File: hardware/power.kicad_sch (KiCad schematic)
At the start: 42 parts, among them J401 61300111121, J402 61300111121, J403 PRPC001DAAN-RC, J404 61300111121, J405 PRPC001DAAN-RC, J406 PRPC001DAAN-RC, J407 61300111121, Q401 BSS806NH, U401 LM66200DRLR, U402 TPS63020DSJR, U403 LD39200DPUR

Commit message: HW: Refactor the schematics
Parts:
- removed C410: 0.1 µF, perfect_footprints:C_0402_1005Metric, symbol Device:C
- removed C411: 10 μF, Capacitor_SMD:C_0603_1608Metric, symbol Device:C
- removed D401: 150141RS73100, LED_SMD:LED_PLCC_2835, symbol Device:LED
- removed J402: 61300111121, Connector_PinHeader_2.54mm:PinHeader_1x01_P2.54mm_Vertical, symbol Connector_Generic:Conn_01x01
- removed J403: PRPC001DAAN-RC, Connector_PinHeader_2.54mm:PinHeader_1x02_P2.54mm_Vertical, symbol Connector_Generic:Conn_01x02
- removed Q401: BSS806NH, Package_TO_SOT_SMD:SOT-23-3, symbol Transistor_FET:Q_NMOS_GSD
- removed R402, R404: 330 Ω, perfect_footprints:R_0402_1005Metric, symbol Device:R
- removed R403: 180 kΩ, perfect_footprints:R_0402_1005Metric, symbol Device:R
- removed R405, R413: 0 Ω, perfect_footprints:R_0402_1005Metric, symbol Device:R
- removed R410: 56 kΩ, perfect_footprints:R_0402_1005Metric, symbol Device:R
- removed R411: 10 kΩ, perfect_footprints:R_0402_1005Metric, symbol Device:R
- removed R412: 4.7 kΩ, perfect_footprints:R_0402_1005Metric, symbol Device:R
- removed TP401: TestPoint, TestPoint:TestPoint_Pad_D1.0mm, symbol Connector:TestPoint
- removed U403: LD39200DPUR, Package_DFN_QFN:DFN-8-1EP_4x4mm_P0.8mm_EP2.3x3.24mm, symbol STMicroelectronics:LD39200DPUR
- added C203, C204: 1 µF, Capacitor_SMD:C_0603_1608Metric, symbol Device:C
- added C301: 100 μF, Capacitor_THT:CP_Radial_D5.0mm_P2.00mm, symbol Device:C_Polarized
- added C302, C305: 0.1 µF, perfect_footprints:C_0402_1005Metric, symbol Device:C
- added C303, C304: 4.7 µF, Capacitor_SMD:C_0603_1608Metric, symbol Device:C
- added D301, D302, D303: 150141RS73100, LED_SMD:LED_PLCC_2835, symbol Device:LED
- added D704: SMAJ5.0A, Diode_SMD:D_SMA, symbol Device:D_Zener
- added D705: DT1240A-08LP3810-7, Package_DFN_QFN:Diodes_UDFN3810-9_TYPE_B, symbol Power_Protection:D3V3X8U9LP3810
- added F201, F301: 1.5A, Fuse:Fuse_0805_2012Metric, symbol Device:Fuse
- added J1: USB4105-GF-A, Connector_USB:USB_C_Receptacle_GCT_USB4105-xx-A_16P_TopMnt_Horizontal, symbol Connector:USB_C_Receptacle_USB2.0_16P
- added J202, J302: PRPC001DAAN-RC, Connector_PinHeader_2.54mm:PinHeader_1x02_P2.54mm_Vertical, symbol Connector_Generic:Conn_01x02
- added J301: B2B-XH-A, Connector_JST:JST_XH_B2B-XH-A_1x02_P2.50mm_Vertical, symbol Connector_Generic:Conn_01x02
- added L301: 1.5 µH, Inductor_SMD:L_Vishay_IHLP-2525, symbol Device:L
- added Q301: IRLML6401TRPBF, Package_TO_SOT_SMD:SOT-23-3, symbol Transistor_FET:Q_PMOS_GSD
- added Q302, Q303: DMN2005, Package_SON:Diodes_PowerDI3333-8, symbol Diodes Incorporated:DMN2005UFG-7
- added R103: 0 Ω, Resistor_SMD:R_1206_3216Metric, symbol Device:R
- added R301: 330 Ω, perfect_footprints:R_0402_1005Metric, symbol Device:R
- added R302: 82 mΩ, Resistor_SMD:R_1206_3216Metric, symbol Device:R
- added R303, R305: 2.2 kΩ, perfect_footprints:R_0402_1005Metric, symbol Device:R
- added R304: 10 kΩ, perfect_footprints:R_0402_1005Metric, symbol Device:R
- added R306, R307, R308: 4.7 kΩ, perfect_footprints:R_0402_1005Metric, symbol Device:R
- added R309: 22 Ω, perfect_footprints:R_0402_1005Metric, symbol Device:R
- added R710, R711: 5.1 kΩ, perfect_footprints:R_0402_1005Metric_HDI, symbol Device:R
- added TP301, TP302, TP404: TestPoint, TestPoint:TestPoint_Pad_D1.0mm, symbol Connector:TestPoint
- added U301: BQ29728DSER, Package_SON:WSON-6_1.5x1.5mm_P0.5mm, symbol Texas Instruments:BQ297xy
- added U302: MCP73833T-FCI/MF, Package_DFN_QFN:DFN-10-1EP_3x3mm_P0.5mm_EP1.58x2.35mm, symbol Battery_Management:MCP73833-xxx-MF
- added U303: MAX17048G+T10, Package_DFN_QFN:TDFN-8-1EP_2x2mm_P0.5mm_EP0.8x1.2mm, symbol Analog Devices:MAX17048
- C409: value 10 μF -> 4.7 µF; DigiKey Part Number 490-12737-1-ND -> 490-7203-1-ND; MPN GRM188R61E106MA73J -> GRM188R61E475KE11D; Size 0603 -> 0402; Tolerance ≤ 20 % -> ≤ 20%; Voltage ≥ 16 V -> ≥ 10 V
- R409: value 1.1 MΩ -> 0 Ω; DigiKey Part Number 732-560112110179CT-ND -> 732-560112110001CT-ND; MPN 560112110179 -> 560112110001; Size (none) -> 0402; Tolerance ≤ 1 % -> (none); now not fitted; now left out of the parts list
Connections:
- net ST is gone; now on net BAT_DETn: R401.2, U401.8 (ST)
- net BAT_DETn: now also C409.1
- net GND: now also C203.2, C204.2, C303.2, C304.2, C305.2, J1.A1 (GND), J1.A12 (GND), J1.B1 (GND), J1.B12 (GND), J202.1 (Pin_1), J302.2 (Pin_2), Q303.1 (S), Q303.2 (S), Q303.3 (S), R303.2, R304.2, R305.2, R710.2, R711.2, U302.11 (EP), U302.5 (V_{SS}), U303.1 (CTG), U303.4 (GND), U303.6 (QSTRT), U303.9 (EP)
- net PS/SYNC: now also R409.1
- net VINA: now also R409.2
- net V_3V3: now also R103.2
- net V_BAT: now also C301.1, C303.1, C305.1, Q301.2 (S), R301.1, TP404.1, U302.10 (V_{BAT}), U302.9 (V_{BAT}), U303.2 (CELL), U303.3 (V_{DD})
- net V_3V3_EN: no longer names the net of U402.14 (PG)
- net V_3V3_EN: no longer R409.2
- net V_3V3_OUT: no longer names the net of J405.1 (Pin_1)
- net V_3V3_OUT: now also C406.1, C407.1, C408.1, R407.1, U402.4 (VOUT), U402.5 (VOUT), R103.1
- removed net V_3V55: C406.1, C407.1, C408.1, C409.1, R407.1, R409.1, U402.4 (VOUT), U402.5 (VOUT)
- net V_5V0 renamed V_BUS
- net V_BUS: now also C204.1, C304.1, D301.2 (A), D302.2 (A), D303.2 (A), J202.2 (Pin_2), L301.2, U302.1 (V_{DD}), U302.2 (V_{DD})
- new net: D303.1 (K), R308.2
- new net: C301.2, C302.2, J301.1 (Pin_1), Q301.1 (G), R302.1, U301.4 (VSS)
- new net: J302.1 (Pin_1), Q302.1 (S), Q302.2 (S), Q302.3 (S), R302.2
- new net: D301.1 (K), R306.2
- new net: C203.1, F201.2, L301.1
- new net: R309.1, U303.5 (~{ALRT})
- new net: F301.2, Q301.3 (D)
- new net: D302.1 (K), R307.2
- new net: Q302.5 (D), Q303.5 (D)
- new net BAT_MON_INTn: R309.2
- new net BAT_PROT_IN: C302.1, R301.2, U301.5 (BAT)
- new net CC1: J1.A5 (CC1), R711.1
- new net CC2: J1.B5 (CC2), R710.1
- new net CHASSIS: D704.2 (A), D705.3 (GND), J1.SH (SHIELD)
- new net C_{OUT}: Q303.4 (G), TP302.1, U301.2 (Cout)
- new net D_{OUT}: Q302.4 (G), TP301.1, U301.3 (Dout)
- new net I2C.SCL: U303.7 (SCL)
- new net I2C.SDA: U303.8 (SDA)
- new net PG: R308.1, U302.7 (~{PG})
- new net PROG: R305.1, U302.6 (PROG)
- new net STAT1: R306.1, U302.3 (STAT1)
- new net STAT2: R307.1, U302.4 (STAT2)
- new net THERM: R304.1, U302.8 (THERM)
- new net USB.DM: D705.1 (Line-1), J1.A7 (D-), J1.B7 (D-)
- new net USB.DP: D705.2 (Line-3), J1.A6 (D+), J1.B6 (D+)
- new net V-: R303.1, U301.6 (V-)
- new net V_BAT_IN: F301.1, J301.2 (Pin_2)
- new net V_BUS_IN: D704.1 (K), F201.1, J1.A4 (VBUS), J1.A9 (VBUS), J1.B4 (VBUS), J1.B9 (VBUS)
- no-connect marks 0 -> 10
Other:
- note added: "Battery"
- note added: "Charging"
- note added: "Debug"
- note added: "Monitoring"
- note added: "Notes"
- note added: "OPT: Bypass protection chip"
- note added: "OPT: External +5V supply"
- note added: "Power path management"
- note added: "Power regulation"
- note added: "Protection"
- note added: "R1"
- note added: "R2"
- note added: "Route USB as 90 Ω differential."
- note added: "USB"
- note removed: "If the board is powered from V_BAT, then ST is pulled high. If the board is powered from V_5V0, then ST is pulled low. BAT_DETn is low when the battery is providing the power. BAT_DETn is high when the USB is providing the power."
- note removed: "Max dropout voltage is 250 mV according to datasheet."
- note removed: "Place close to LDO."
- note removed: "Place the header near the test points for the oscilloscope ground."
- note removed: "Power path management If V_BAT > V_5V0, V_{OUT} = V_BAT If V_5V0 > V_BAT, V_{OUT} = V_5V0"
- note removed: "Testing: For current measurements, populate the header and remove the 0 Ω jumper."
- note removed: "Testing: Power-saving mode should be enabled but if it doesn't work, provide an easy way to disable it."
- note removed: "Use a common center pad."
- note removed: "V_{OUT} will be 3.55 V, which is just enough for the LDO."
- moved on the sheet: C401, C402, C403, C404, C405, C406, C407, C408, D402, J401, J404, J405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

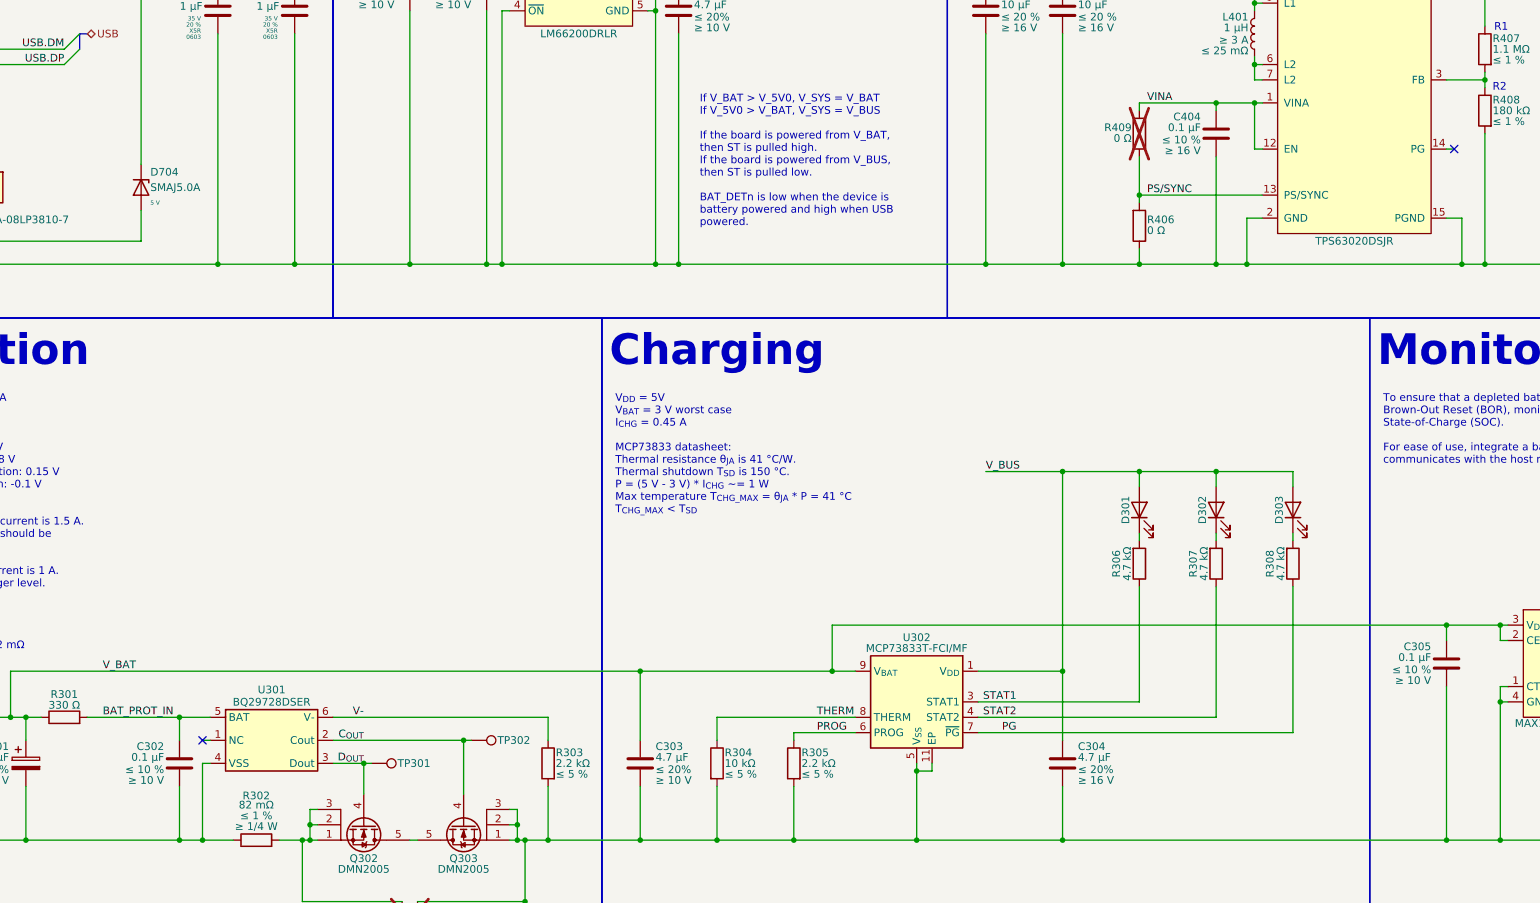
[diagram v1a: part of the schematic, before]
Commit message: Add EEPROM
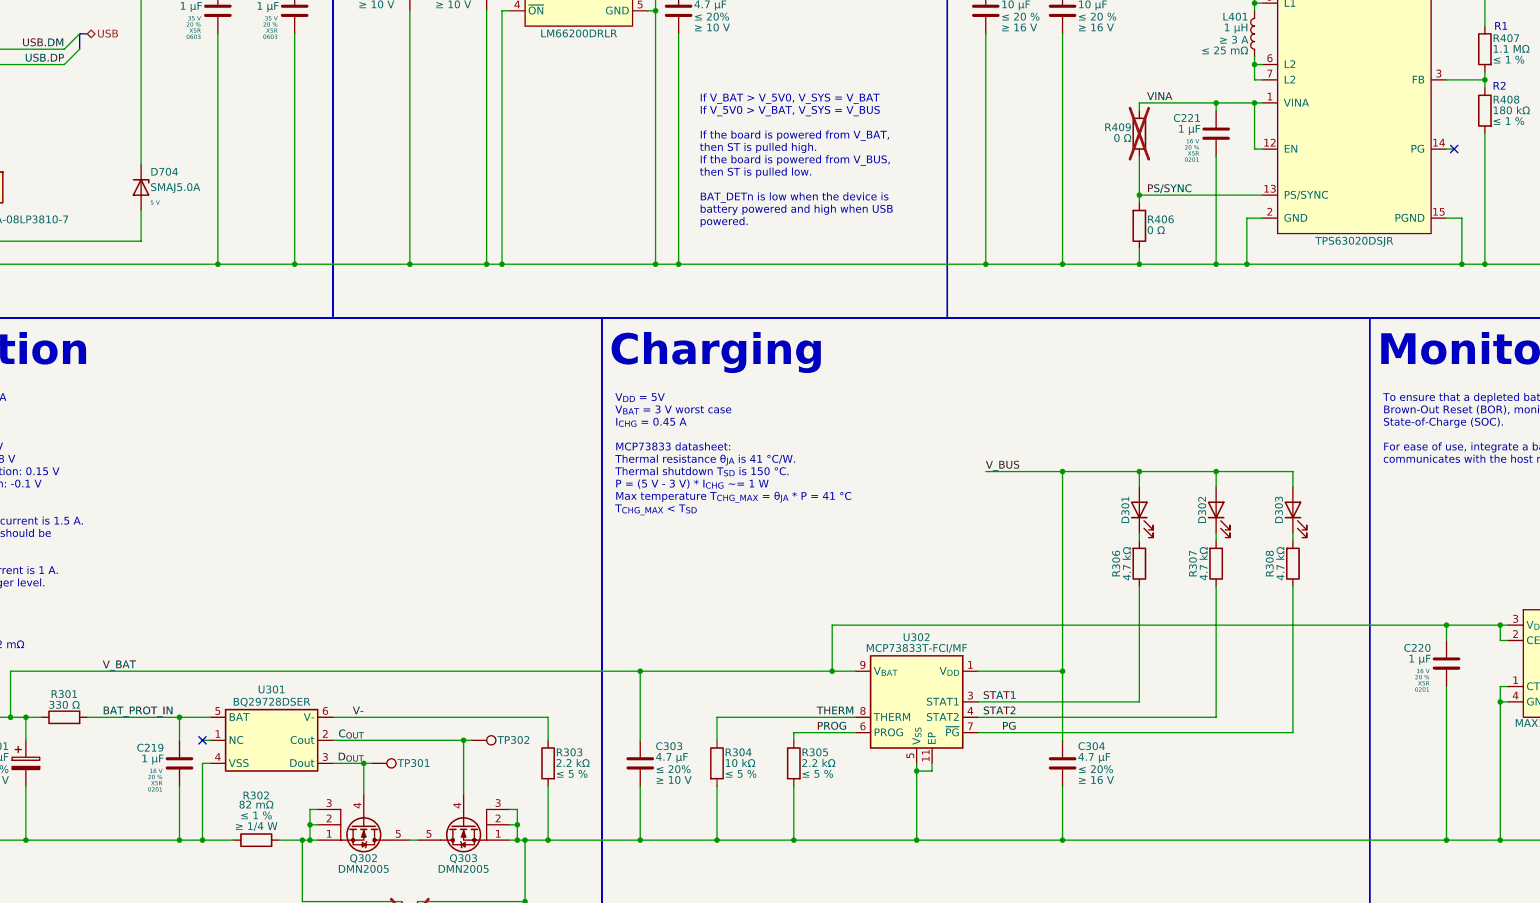
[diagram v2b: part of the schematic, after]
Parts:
- removed C302, C305, C404: 0.1 µF, perfect_footprints:C_0402_1005Metric, symbol Device:C
- added C219, C220, C221: 1 µF, perfect_footprints:C_0201_0603Metric, symbol Device:C
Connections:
- net BAT_PROT_IN: now also C219.1
- net GND: now also C220.2, C221.2
- net VINA: now also C221.1
- net V_BAT: now also C220.1
- net at C301.2, J301.1 (Pin_1), Q301.1 (G)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: now also C219.2

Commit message: Refine schematics
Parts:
- removed C203: 1 µF, Capacitor_SMD:C_0603_1608Metric, symbol Device:C
- removed C301: 100 μF, Capacitor_THT:CP_Radial_D5.0mm_P2.00mm, symbol Device:C_Polarized
- removed C303, C304, C401, C402, C409: 4.7 µF, Capacitor_SMD:C_0603_1608Metric, symbol Device:C
- removed C403, C405: 10 μF, Capacitor_SMD:C_0603_1608Metric, symbol Device:C
- removed C406, C407, C408: 22 μF, Capacitor_SMD:C_0603_1608Metric, symbol Device:C
- removed F201, F301: 1.5A, Fuse:Fuse_0805_2012Metric, symbol Device:Fuse
- removed L401: 1 µH, Inductor_SMD:L_Wuerth_MAPI-4030, symbol Device:L
- removed R301: 330 Ω, perfect_footprints:R_0402_1005Metric, symbol Device:R
- removed R302: 82 mΩ, Resistor_SMD:R_1206_3216Metric, symbol Device:R
- removed R303, R305, R414: 2.2 kΩ, perfect_footprints:R_0402_1005Metric, symbol Device:R
- removed R304: 10 kΩ, perfect_footprints:R_0402_1005Metric, symbol Device:R
- removed R306, R307, R308: 4.7 kΩ, perfect_footprints:R_0402_1005Metric, symbol Device:R
- removed R309: 22 Ω, perfect_footprints:R_0402_1005Metric, symbol Device:R
- removed R401, R408: 180 kΩ, perfect_footprints:R_0402_1005Metric, symbol Device:R
- removed R406, R409: 0 Ω, perfect_footprints:R_0402_1005Metric, symbol Device:R
- removed R407: 1.1 MΩ, perfect_footprints:R_0402_1005Metric, symbol Device:R
- added C1: 100 µF, Capacitor_THT:CP_Radial_D5.0mm_P2.50mm, symbol Device:C_Polarized
- added C10, C4, C9: 10 µF, Capacitor_SMD:C_0603_1608Metric, symbol Device:C
- added C11, C5, C6, C7, C8: 4.7 µF, perfect_footprints:C_0402_1005Metric_HDI, symbol Device:C
- added C14, C15, C16: 22 µF, Capacitor_SMD:C_0603_1608Metric, symbol Device:C
- added D1, D2: SMAJ5.0A, Diode_SMD:D_SMA, symbol Device:D_Zener
- added F1, F2: 1.5 A, Fuse:Fuse_0805_2012Metric, symbol Device:Fuse
- added L2: 1 µH, Inductor_SMD:L_Wuerth_MAPI-4030, symbol Device:L
- added R10, R13, R14, R15, R16, R7: 2.2 kΩ, perfect_footprints:R_0201_0603Metric, symbol Device:R
- added R11, R12: 0 Ω, perfect_footprints:R_0201_0603Metric, symbol Device:R
- added R17: 1.1 MΩ, perfect_footprints:R_0201_0603Metric, symbol Device:R
- added R18, R8: 180 kΩ, perfect_footprints:R_0201_0603Metric, symbol Device:R
- added R19: 27 Ω, perfect_footprints:R_0201_0603Metric, symbol Device:R
- added R5: 330 Ω, perfect_footprints:R_0402_1005Metric, symbol Device:R
- added R6: 82 mΩ, Resistor_SMD:R_1206_3216Metric, symbol Device:R
- added R9: 10 kΩ, perfect_footprints:R_0201_0603Metric, symbol Device:R
- L1: renamed from L301; Size (none) -> IHLP-2525
- renumbered C221 to C12, C220 to C13, C219 to C2, C204 to C3, D705 to D3, D704 to D4, D301 to D5, D402 to D6, D302 to D7, D303 to D8, J301 to J1, J1 to J2, J302 to J3, J202 to J4, J401 to J5, J404 to J6, J407 to J7, J406 to J8, J405 to J9, Q301 to Q1, Q302 to Q2, Q303 to Q3, R103 to R20, R710 to R3, R711 to R4, TP301 to TP1, TP302 to TP2, TP402 to TP3, TP403 to TP4, TP404 to TP5, U301 to U1, U401 to U2, U302 to U3, U402 to U4, U303 to U5
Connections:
- net BAT_DETn: now also C8.1, R8.2
- net BAT_MON_INTn: now also R19.2
- net BAT_PROT_IN: now also R5.2
- net CHASSIS: now also D1.2 (A), D2.2 (A)
- net GND: now also C10.2, C11.2, C14.2, C15.2, C16.2, C4.2, C5.2, C6.2, C7.2, C8.2, C9.2, R10.2, R12.2, R14.2, R18.2, R7.2, R9.2
- net PG: now also R16.2
- net PROG: now also R10.1
- net PS/SYNC: now also R11.2, R12.1
- net STAT1: now also R13.2
- net STAT2: now also R15.2
- net THERM: now also R9.1
- net V-: now also R7.1
- net VINA: now also R11.1
- net V_BAT: now also C1.1, C6.1, C7.1, R5.1, R8.1
- net V_BAT_IN: now also D2.1 (K), F1.1
- net V_BUS: now also C11.1, C4.1, C5.1; no longer C3.1
- net V_BUS_IN: now also F2.1
- net V_SYS: now also C10.1, C9.1
- net at J9.1 (Pin_1), R20.1, U4.4 (VOUT)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: now also C14.1, C15.1, C16.1, R17.1
- net at D8.1 (K): now also R16.1
- net at C2.2, J1.1 (Pin_1), Q1.1 (G)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: now also C1.2, D1.1 (K), R6.1
- net at J3.1 (Pin_1), Q2.1 (S), Q2.2 (S)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: now also R6.2
- net at D5.1 (K): now also R13.1
- net at L1.1: now also C3.1, F2.2
- net at U4.3 (FB): now also R17.2, R18.1
- net at U5.5 (~{ALRT}): now also R19.1
- net at Q1.3 (D): now also F1.2
- net at D6.1 (K): now also R14.1
- net at U4.6 (L2), U4.7 (L2): now also L2.1
- net at U4.8 (L1), U4.9 (L1): now also L2.2
- net at D7.1 (K): now also R15.1
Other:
- moved on the sheet: C13, C3, U5

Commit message: HW: Refine PDN
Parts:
- removed C3: 1 µF, Capacitor_SMD:C_0603_1608Metric, symbol Device:C
- removed F1: 1.5 A, Fuse:Fuse_0805_2012Metric, symbol Device:Fuse
- removed L1: 1.5 µH, Inductor_SMD:L_Vishay_IHLP-2525, symbol Device:L
- added C57: 10 µF, Capacitor_SMD:C_0603_1608Metric, symbol Device:C
- added F3: 1.5 A, Fuse:Fuse_0805_2012Metric, symbol Device:Fuse
- added R87: 0 Ω, Resistor_SMD:R_0805_2012Metric, symbol Device:R
- R17: value 1.1 MΩ -> 1.02 MΩ
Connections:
- net GND: now also C57.2
- net V_BAT_IN: now also F3.1
- net V_BUS: now also C57.1, R87.2; no longer C4.1
- net V_OUT: now reaches C14.1, C15.1, C16.1, J9.1 (Pin_1), R17.1, R20.1, U4.4 (VOUT), U4.5 (VOUT)
- net at F2.2: now also C4.1, R87.1
- net at Q1.3 (D): now also F3.2
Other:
- note added: "Ferrite placeholder"
- moved on the sheet: C4, C5, C6, D3, D4, F2, R3, R4

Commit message: HW: Refine schematics
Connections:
- net BAT_DETn renamed ST
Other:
- note added: "USB-C"
- note removed: "USB"
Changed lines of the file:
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@@
 		)
 	)
-	(text "USB"
+	(text "USB-C"
 		(exclude_from_sim no)
 		(at 13.97 40.64 0)
@@
 		)
 	)
-	(text_box "If V_BAT > V_5V0, V_SYS = V_BAT\nIf V_5V0 > V_BAT, V_SYS = V_BUS\n\nIf the board is powered from V_BAT, then ST is pulled high.\nIf the board is powered from V_BUS, then ST is pulled low.\n\nBAT_DETn is low when the device is battery powered and high when USB powered."
+	(text_box "If V_BAT > V_5V0, V_SYS = V_BAT\nIf V_5V0 > V_BAT, V_SYS = V_BUS\n\nIf the board is powered from V_BAT, then ST is pulled high.\n\nIf the board is powered from V_BUS, then ST is pulled low."
 		(exclude_from_sim no)
 		(at 205.74 88.9 0)
-		(size 39.37 24.3946)
+		(size 35.56 20.3199)
 		(margins 0.9525 0.9525 0.9525 0.9525)
 		(stroke
@@
 		)
 	)
+	(text_box "The USB-C interface can be used to power the board, charge the battery and communicate with the microcontroller.\n\nWith 5.1 k pull-downs on the CC lines, the device is advertised as a downstream device.\n\nNOTE: The device can momentarily draw more than 500 mA so a USB-C to USB-A cable might not suffice."
+		(exclude_from_sim no)
+		(at 50.8 39.37 0)
+		(size 48.26 24.13)
+		(margins 0.9525 0.9525 0.9525 0.9525)
+		(stroke
+			(width -0.0001)
+			(type solid)
+		)
+		(fill
+			(type none)
+		)
+		(effects
+			(font
+				(size 1.27 1.27)
+			)
+			(justify left top)
+		)
+	)
 	(text_box "Power"
 		(exclude_from_sim no)
@@
 		)
 	)
-	(hierarchical_label "BAT_DETn"
+	(hierarchical_label "ST"
 		(shape output)
 		(at 210.82 71.12 0)
